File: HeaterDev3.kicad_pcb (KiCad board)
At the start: 2 copper layers, 108 x 76.2 mm, 38 parts, among them J1 USB_C_Receptacle_USB2.0, J9 Conn_01x04_Female, Q1 Q_NMOS_GDS, SW1 SW_SPST, U1 ATSAMD21E18A-MU, U2 FUSB302BMPX, U3 STS-30-DIS, U4 LM393, U5 AP2112K-3.3

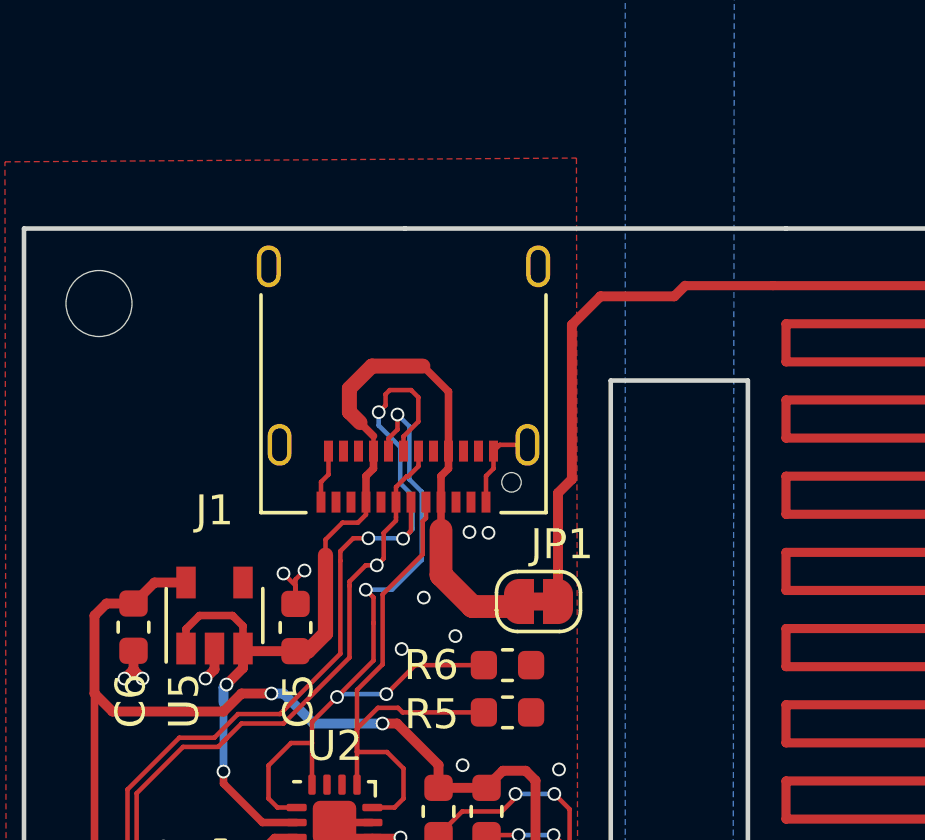
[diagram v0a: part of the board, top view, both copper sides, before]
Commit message: Cleaned up routing.
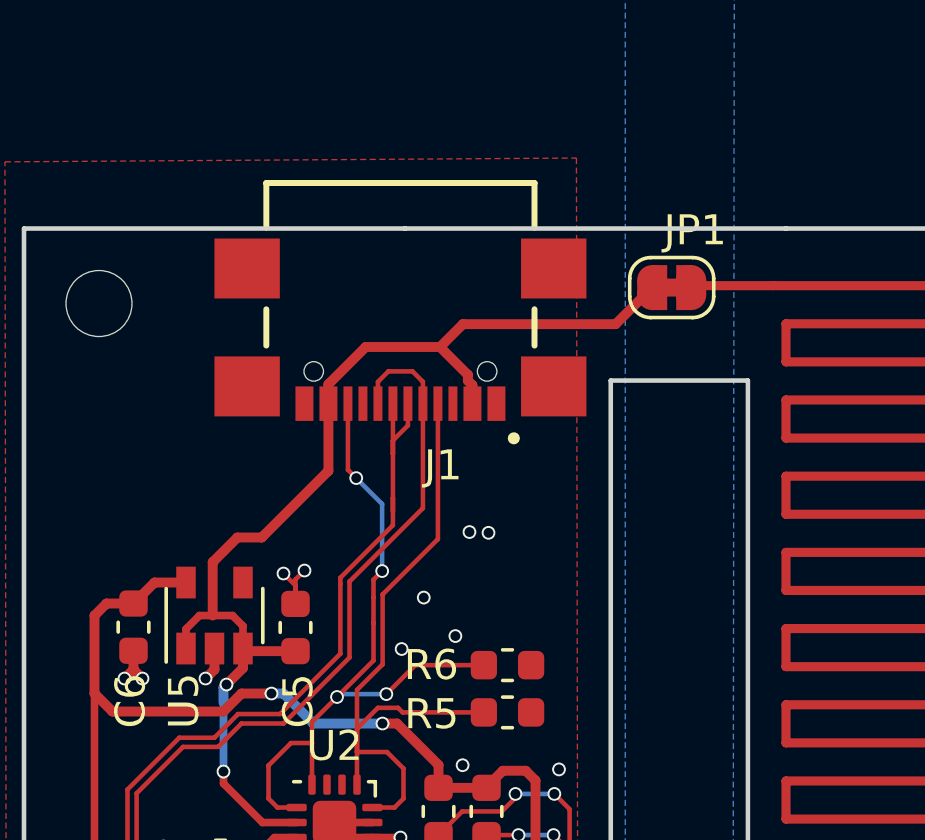
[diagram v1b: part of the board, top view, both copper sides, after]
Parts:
- J1: value USB_C_Receptacle_USB2.0 -> USB4110-GF-A; footprint Connector_USB:USB_C_Receptacle_Amphenol_12401610E4-2A -> HeaterDev3:GCT_USB4110-GF-A
- moved JP1 11.4 mm to (-73.7, -74.2)
- moved J1 0.67 mm to (-82.7, -71.4)
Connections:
- J1 pad A7: D- -> D+
- J1 pad B6: D+ -> D-
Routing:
- net /COIL: track 4515.2 -> 4497.6 mm
- net GND: track 61.4 -> 56.6 mm
- net D-: track 27.5 -> 32.2 mm, vias 1 -> 0
- net D+: track 35.1 -> 30.7 mm, vias 3 -> 0
- net CC1: track 19.7 -> 23.1 mm
- net CC2: track 25.5 -> 23.4 mm
